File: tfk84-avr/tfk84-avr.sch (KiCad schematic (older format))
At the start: 43 parts, among them J1 USB_C_Receptacle_USB2.0, J2 AVR-ISP-6, SW1 Reset, U1 ATmega32U4-AU, Y1 16MHz

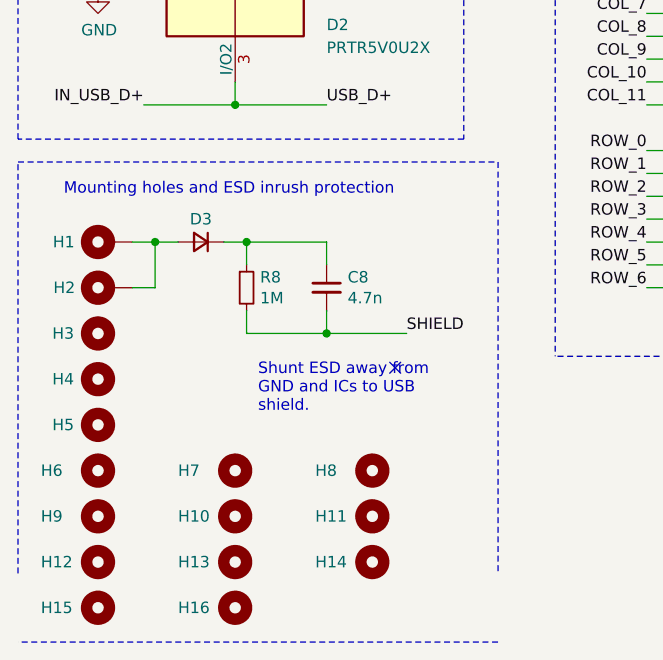
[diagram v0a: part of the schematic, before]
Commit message: Tweak holes
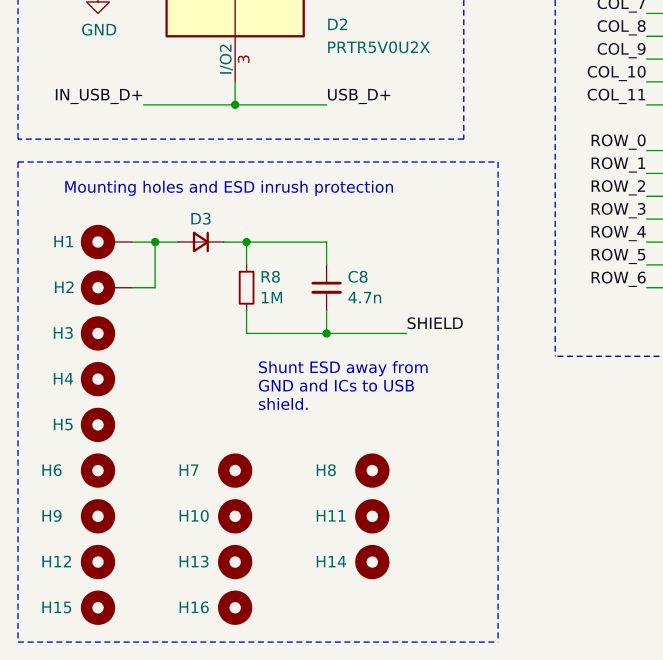
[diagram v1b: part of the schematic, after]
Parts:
- H1, H2: footprint random-keyboard-parts:MountingHole_2.5mm_Pad_TopOnly_NoCrtYd -> MountingHole:MountingHole_2.5mm_Pad
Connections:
- no-connect marks 4 -> 3
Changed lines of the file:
@@
 Wire Notes Line
 	700  5600 2800 5600
-Wire Notes Line
-	2800 5600 2800 7400
-Wire Notes Line
-	2800 7700 700  7700
-Wire Notes Line
-	700  7400 700  5600
 Wire Wire Line
 	1400 5950 1300 5950
@@
 F 0 "H1" V 1100 6150 50  0000 C CNN
 F 1 "Case" V 1000 6150 50  0001 C CNN
-F 2 "random-keyboard-parts:MountingHole_2.5mm_Pad_TopOnly_NoCrtYd" H 1100 5950 50  0001 C CNN
+F 2 "MountingHole:MountingHole_2.5mm_Pad" H 1100 5950 50  0001 C CNN
 F 3 "~" H 1100 5950 50  0001 C CNN
 	1    1100 5950
@@
 F 0 "H2" V 1100 6300 50  0000 L CNN
 F 1 "Case" V 1000 6250 50  0001 L CNN
-F 2 "random-keyboard-parts:MountingHole_2.5mm_Pad_TopOnly_NoCrtYd" H 1100 6150 50  0001 C CNN
+F 2 "MountingHole:MountingHole_2.5mm_Pad" H 1100 6150 50  0001 C CNN
 F 3 "~" H 1100 6150 50  0001 C CNN
 	1    1100 6150
@@
 	1    0    0    -1
 $EndComp
-NoConn ~ 2350 6500
 $Comp
 L Mechanical:MountingHole H12
@@
 	1    0    0    -1
 $EndComp
+Wire Notes Line
+	700  5600 700  7700
+Wire Notes Line
+	2800 5600 2800 7700
+Wire Notes Line
+	700  7700 2800 7700
 $EndSCHEMATC
